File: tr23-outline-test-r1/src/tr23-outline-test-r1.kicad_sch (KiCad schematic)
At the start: 34 parts, among them SW1 REV_TACT, SW10 REV_TACT, SW11 REV_TACT, SW12 REV_TACT, SW13 REV_TACT, SW14 REV_TACT, SW15 REV_TACT, SW16 REV_TACT, SW17 REV_TACT, SW18 REV_TACT, SW19 REV_TACT, SW2 REV_TACT, SW20 REV_TACT, SW21 REV_TACT, SW22 REV_TACT, SW23 REV_TACT, SW24 REV_TACT, SW25 REV_TACT, SW26 REV_TACT, SW27 REV_TACT, SW28 REV_TACT, SW29 REV_TACT, SW3 REV_TACT, SW30 REV_TACT, SW31 REV_TACT, SW32 REV_TACT, SW33 REV_TACT, SW34 REV_TACT, SW4 REV_TACT, SW5 REV_TACT, SW6 REV_TACT, SW7 REV_TACT, SW8 REV_TACT, SW9 REV_TACT

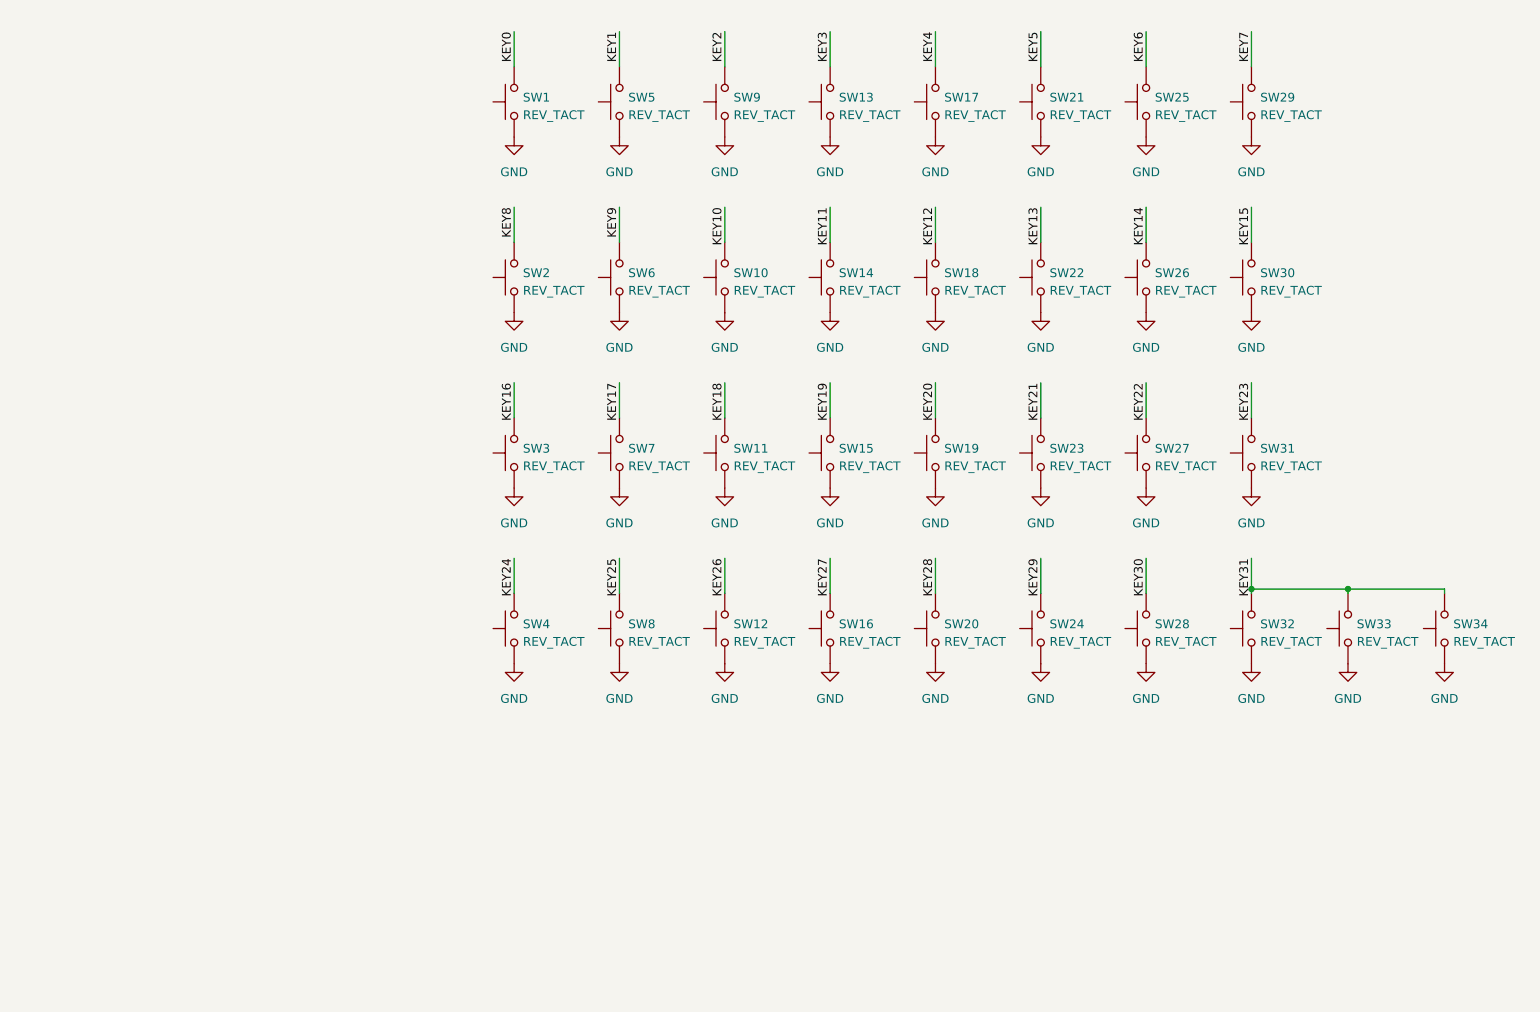
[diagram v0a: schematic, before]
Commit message: Update SVG export
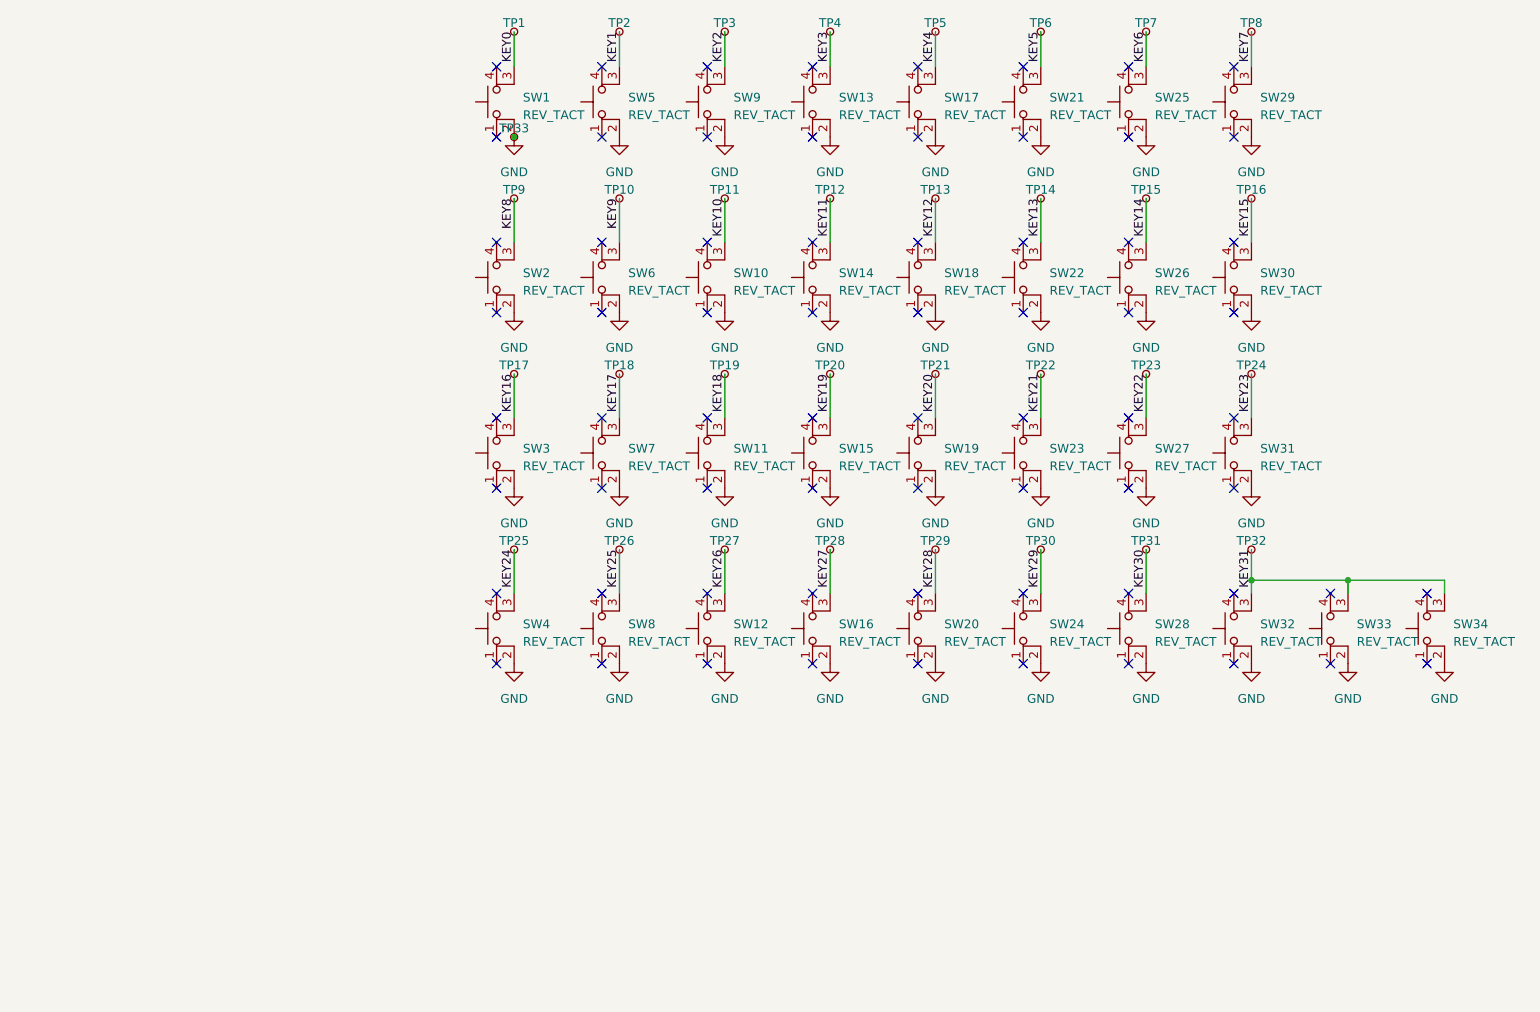
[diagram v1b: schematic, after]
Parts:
- added TP1, TP10, TP11, TP12, TP13, TP14, TP15, TP16, TP17, TP18, TP19, TP2, TP20, TP21, TP22, TP23, TP24, TP25, TP26, TP27, TP28, TP29, TP3, TP30, TP31, TP32, TP33, TP4, TP5, TP6, TP7, TP8, TP9: ~, TestPoint:TestPoint_Pad_D1.5mm, symbol Connector:TestPoint_Small
- SW1, SW10, SW11, SW12, SW13, SW14, SW15, SW16, SW17, SW18, SW19, SW2, SW20, SW21, SW22, SW23, SW24, SW25, SW26, SW27, SW28, SW29, SW3, SW30, SW31, SW32, SW33, SW34, SW4, SW5, SW6, SW7, SW8, SW9: symbol Switch:SW_MEC_5G -> Switch:SW_MEC_5E
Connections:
- net GND: now also TP33.1; no longer SW1.1 (A), SW10.1 (A), SW11.1 (A), SW12.1 (A), SW13.1 (A), SW14.1 (A), SW15.1 (A), SW16.1 (A), SW17.1 (A), SW18.1 (A), SW19.1 (A), SW2.1 (A), SW20.1 (A), SW21.1 (A), SW22.1 (A), SW23.1 (A), SW24.1 (A), SW25.1 (A), SW26.1 (A), SW27.1 (A), SW28.1 (A), SW29.1 (A), SW3.1 (A), SW30.1 (A), SW31.1 (A), SW32.1 (A), SW33.1 (A), SW34.1 (A), SW4.1 (A), SW5.1 (A), SW6.1 (A), SW7.1 (A), SW8.1 (A), SW9.1 (A)
- net KEY0: now also TP1.1; no longer SW1.4 (B)
- net KEY1: now also TP2.1; no longer SW5.4 (B)
- net KEY10: now also TP11.1; no longer SW10.4 (B)
- net KEY11: now also TP12.1; no longer SW14.4 (B)
- net KEY12: now also TP13.1; no longer SW18.4 (B)
- net KEY13: now also TP14.1; no longer SW22.4 (B)
- net KEY14: now also TP15.1; no longer SW26.4 (B)
- net KEY15: now also TP16.1; no longer SW30.4 (B)
- net KEY16: now also TP17.1; no longer SW3.4 (B)
- net KEY17: now also TP18.1; no longer SW7.4 (B)
- net KEY18: now also TP19.1; no longer SW11.4 (B)
- net KEY19: now also TP20.1; no longer SW15.4 (B)
- net KEY2: now also TP3.1; no longer SW9.4 (B)
- net KEY20: now also TP21.1; no longer SW19.4 (B)
- net KEY21: now also TP22.1; no longer SW23.4 (B)
- net KEY22: now also TP23.1; no longer SW27.4 (B)
- net KEY23: now also TP24.1; no longer SW31.4 (B)
- net KEY24: now also TP25.1; no longer SW4.4 (B)
- net KEY25: now also TP26.1; no longer SW8.4 (B)
- net KEY26: now also TP27.1; no longer SW12.4 (B)
- net KEY27: now also TP28.1; no longer SW16.4 (B)
- net KEY28: now also TP29.1; no longer SW20.4 (B)
- net KEY29: now also TP30.1; no longer SW24.4 (B)
- net KEY3: now also TP4.1; no longer SW13.4 (B)
- net KEY30: now also TP31.1; no longer SW28.4 (B)
- net KEY31: now also TP32.1; no longer SW32.4 (B), SW33.4 (B), SW34.4 (B)
- net KEY4: now also TP5.1; no longer SW17.4 (B)
- net KEY5: now also TP6.1; no longer SW21.4 (B)
- net KEY6: now also TP7.1; no longer SW25.4 (B)
- net KEY7: now also TP8.1; no longer SW29.4 (B)
- net KEY8: now also TP9.1; no longer SW2.4 (B)
- net KEY9: now also TP10.1; no longer SW6.4 (B)
- no-connect marks 0 -> 68

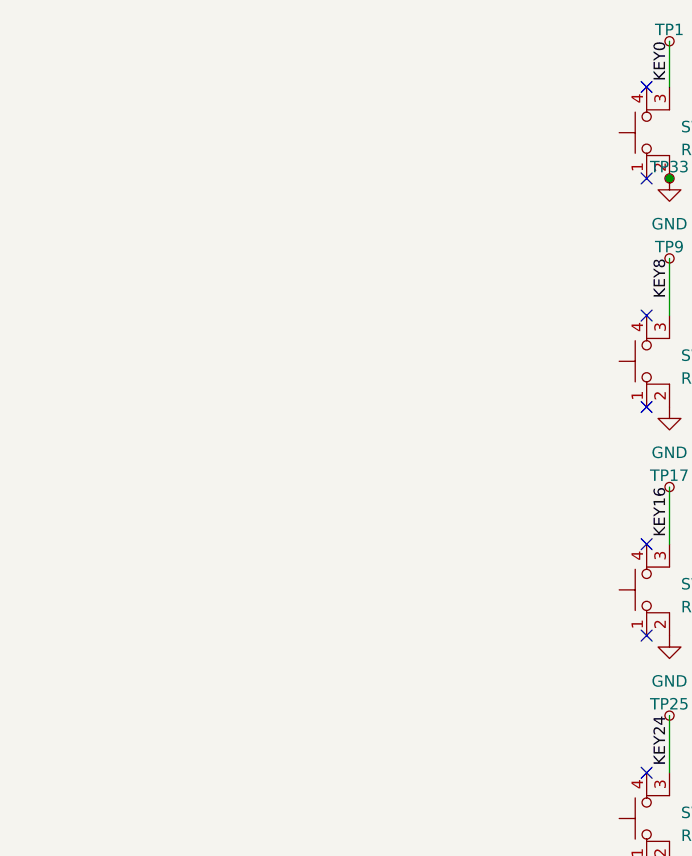
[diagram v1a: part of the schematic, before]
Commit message: Add navigation switches and SAO connector to schematic.
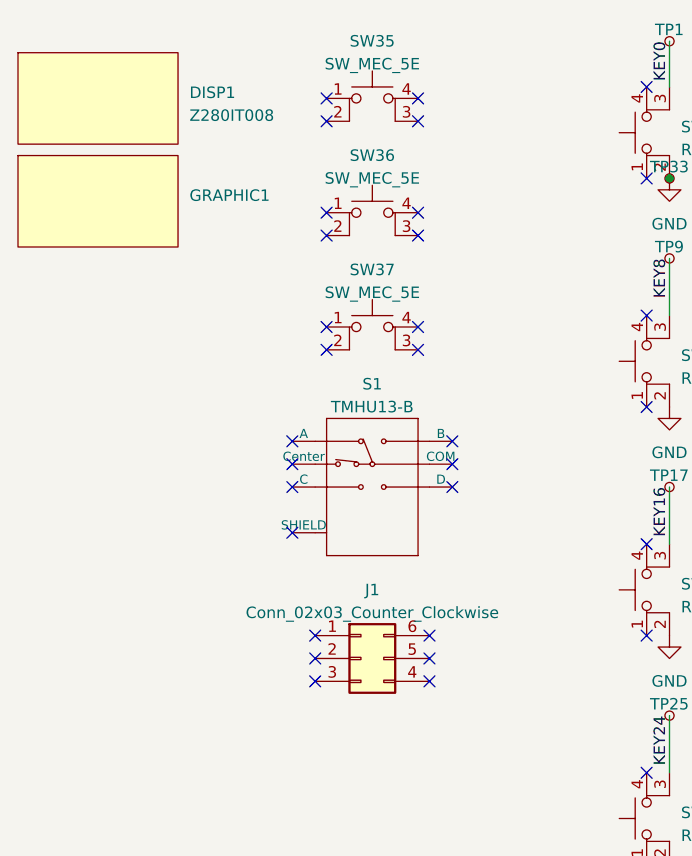
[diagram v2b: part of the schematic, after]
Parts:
- added DISP1: Z280IT008, jeffmakes-kicad-library:Z280IT009, symbol j_Display:Display_dummy
- added GRAPHIC1: (no value), tr23-svg2sz:tr23-r1-svg2sz, symbol j_Display:Display_dummy
- added J1: Conn_02x03_Counter_Clockwise, jeffmakes-kicad-library:PinSocket_2x03_P2.54mm_Through-Board-Mating, symbol Connector_Generic:Conn_02x03_Counter_Clockwise
- added S1: TMHU13-B, jeffmakes-kicad-library:SW_JS1400BFQ, symbol j_Switch:TMHU13-B
- added SW35, SW36, SW37: SW_MEC_5E, jeffmakes-kicad-library:SW_SPST_TACT-6x6-no-silk, symbol Switch:SW_MEC_5E
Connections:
- new net: S1.SH1 (SHIELD), S1.SH2 (SHIELD)
- no-connect marks 68 -> 93

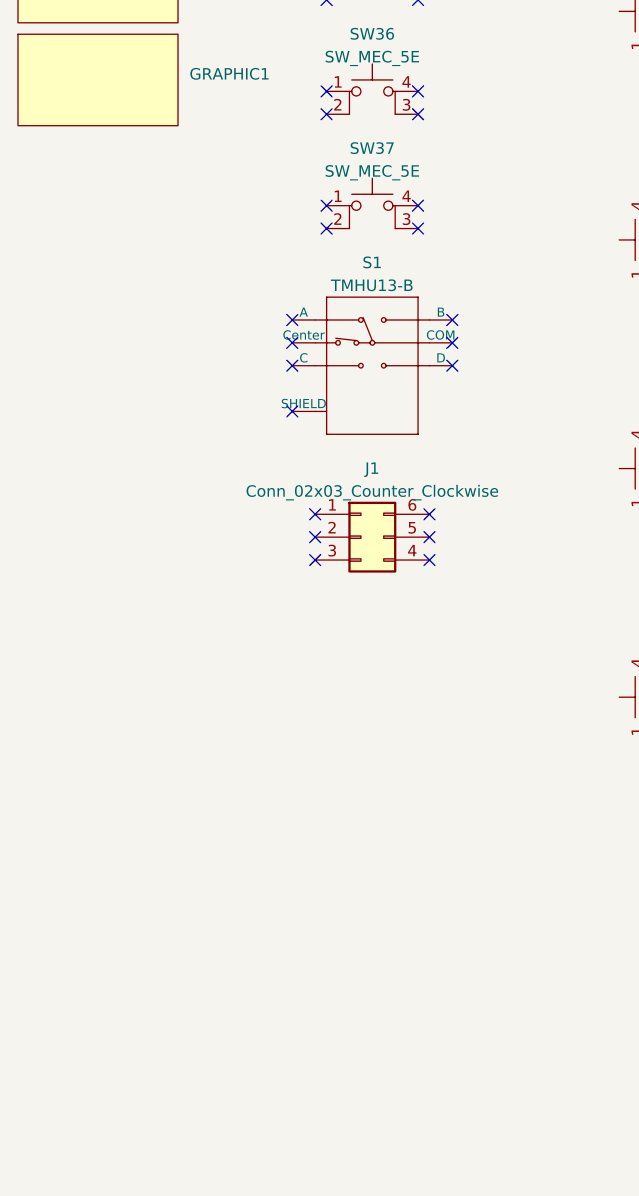
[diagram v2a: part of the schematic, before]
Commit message: Add FFC connector for display.
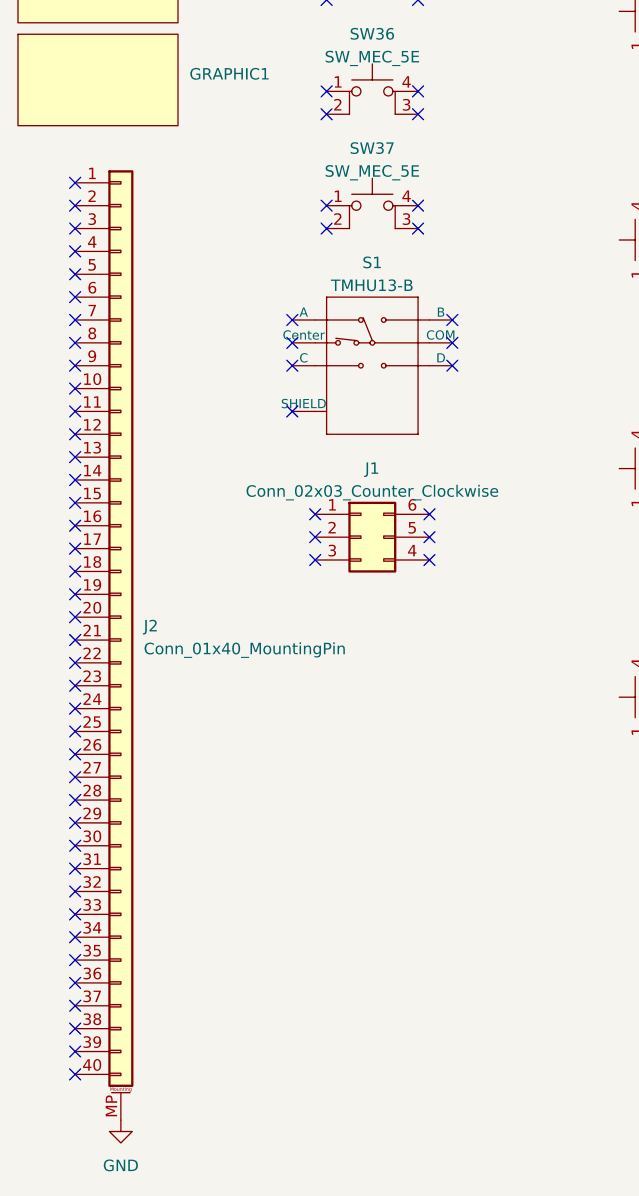
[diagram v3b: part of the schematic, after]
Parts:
- added J2: Conn_01x40_MountingPin, jeffmakes-kicad-library:AFC07x40-1MP_P0.5mm_Horizontal, symbol Connector_Generic_MountingPin:Conn_01x40_MountingPin
- GRAPHIC1: value (none) -> ~
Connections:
- net GND: now also J2.MP (MountPin)
- no-connect marks 93 -> 133
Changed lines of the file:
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@@
   (junction (at 92.71 58.42) (diameter 0) (color 0 0 0 0)
   )
+  (no_connect (at 26.67 82.55))
+  (no_connect (at 26.67 100.33))
   (no_connect (at 210.82 124.46))
   (no_connect (at 53.34 109.22))
@@
   (no_connect (at 196.85 109.22))
   (no_connect (at 50.8 87.63))
+  (no_connect (at 26.67 125.73))
   (no_connect (at 68.58 87.63))
   (no_connect (at 166.37 83.82))
+  (no_connect (at 26.67 77.47))
   (no_connect (at 90.17 58.42))
   (no_connect (at 105.41 109.22))
@@
   (no_connect (at 50.8 90.17))
   (no_connect (at 196.85 99.06))
+  (no_connect (at 26.67 156.21))
   (no_connect (at 105.41 83.82))
   (no_connect (at 66.04 111.76))
+  (no_connect (at 26.67 153.67))
   (no_connect (at 210.82 134.62))
   (no_connect (at 105.41 73.66))
@@
   (no_connect (at 135.89 134.62))
   (no_connect (at 90.17 73.66))
+  (no_connect (at 26.67 102.87))
   (no_connect (at 196.85 48.26))
+  (no_connect (at 26.67 161.29))
   (no_connect (at 54.61 77.47))
   (no_connect (at 151.13 83.82))
+  (no_connect (at 26.67 166.37))
   (no_connect (at 135.89 99.06))
   (no_connect (at 120.65 124.46))
@@
   (no_connect (at 151.13 73.66))
   (no_connect (at 64.77 74.93))
+  (no_connect (at 26.67 90.17))
+  (no_connect (at 26.67 85.09))
+  (no_connect (at 26.67 74.93))
   (no_connect (at 64.77 52.07))
   (no_connect (at 166.37 134.62))
   (no_connect (at 196.85 58.42))
   (no_connect (at 166.37 99.06))
+  (no_connect (at 26.67 92.71))
+  (no_connect (at 26.67 133.35))
   (no_connect (at 53.34 114.3))
+  (no_connect (at 26.67 87.63))
   (no_connect (at 181.61 134.62))
   (no_connect (at 120.65 109.22))
+  (no_connect (at 26.67 123.19))
   (no_connect (at 66.04 109.22))
   (no_connect (at 90.17 83.82))
   (no_connect (at 90.17 134.62))
+  (no_connect (at 26.67 151.13))
   (no_connect (at 181.61 109.22))
+  (no_connect (at 26.67 168.91))
+  (no_connect (at 26.67 113.03))
   (no_connect (at 151.13 124.46))
   (no_connect (at 181.61 99.06))
+  (no_connect (at 26.67 148.59))
   (no_connect (at 64.77 64.77))
   (no_connect (at 135.89 83.82))
@@
   (no_connect (at 105.41 134.62))
   (no_connect (at 54.61 62.23))
+  (no_connect (at 26.67 143.51))
+  (no_connect (at 26.67 128.27))
+  (no_connect (at 26.67 110.49))
   (no_connect (at 166.37 58.42))
+  (no_connect (at 26.67 140.97))
+  (no_connect (at 26.67 80.01))
   (no_connect (at 120.65 134.62))
   (no_connect (at 166.37 124.46))
   (no_connect (at 90.17 48.26))
+  (no_connect (at 26.67 105.41))
   (no_connect (at 105.41 99.06))
   (no_connect (at 135.89 58.42))
@@
   (no_connect (at 135.89 109.22))
   (no_connect (at 64.77 77.47))
+  (no_connect (at 26.67 146.05))
+  (no_connect (at 26.67 130.81))
+  (no_connect (at 26.67 163.83))
   (no_connect (at 68.58 90.17))
+  (no_connect (at 26.67 135.89))
   (no_connect (at 54.61 52.07))
   (no_connect (at 90.17 109.22))
   (no_connect (at 181.61 124.46))
+  (no_connect (at 26.67 118.11))
   (no_connect (at 66.04 114.3))
+  (no_connect (at 26.67 107.95))
   (no_connect (at 151.13 109.22))
   (no_connect (at 135.89 124.46))
+  (no_connect (at 26.67 95.25))
   (no_connect (at 151.13 99.06))
   (no_connect (at 120.65 83.82))
+  (no_connect (at 26.67 171.45))
+  (no_connect (at 26.67 138.43))
   (no_connect (at 135.89 48.26))
   (no_connect (at 224.79 134.62))
@@
   (no_connect (at 54.61 49.53))
   (no_connect (at 64.77 62.23))
+  (no_connect (at 26.67 158.75))
   (no_connect (at 181.61 48.26))
+  (no_connect (at 26.67 115.57))
+  (no_connect (at 26.67 97.79))
   (no_connect (at 120.65 48.26))
   (no_connect (at 151.13 58.42))
   (no_connect (at 166.37 73.66))
+  (no_connect (at 26.67 120.65))
+  (no_connect (at 26.67 72.39))
   (wire (pts (xy 92.71 92.71) (xy 92.71 99.06))
     (stroke (width 0) (type default))
@@
       (effects (font (size 1.27 1.27)) (justify left))
     )
-    (property "Value" "" (at 39.37 62.865 0)
+    (property "Value" "~" (at 39.37 62.865 0)
       (effects (font (size 1.27 1.27)) (justify left))
     )
@@
         )
       )
+    )
+  )
+  (symbol (lib_id "Connector_Generic_MountingPin:Conn_01x40_MountingPin") (at 31.75 120.65 0) (unit 1)
+    (in_bom yes) (on_board yes) (dnp no) (fields_autoplaced)
+    (property "Reference" "J2" (at 34.29 121.6406 0)
+      (effects (font (size 1.27 1.27)) (justify left))
+    )
+    (property "Value" "Conn_01x40_MountingPin" (at 34.29 124.1806 0)
+      (effects (font (size 1.27 1.27)) (justify left))
+    )
+    (property "Footprint" "jeffmakes-kicad-library:AFC07x40-1MP_P0.5mm_Horizontal" (at 31.75 120.65 0)
+      (effects (font (size 1.27 1.27)) hide)
+    )
+    (property "Datasheet" "~" (at 31.75 120.65 0)
+      (effects (font (size 1.27 1.27)) hide)
+    )
+    (pin "1")
+    (pin "10")
+    (pin "11")
+    (pin "12")
+    (pin "13")
+    (pin "14")
+    (pin "15")
+    (pin "16")
+    (pin "17")
+    (pin "18")
+    (pin "19")
+    (pin "2")
+    (pin "20")
+    (pin "21")
+    (pin "22")
+    (pin "23")
+    (pin "24")
+    (pin "25")
+    (pin "26")
+    (pin "27")
+    (pin "28")
+    (pin "29")
+    (pin "3")
+    (pin "30")
+    (pin "31")
+    (pin "32")
+    (pin "33")
+    (pin "34")
+    (pin "35")
+    (pin "36")
+    (pin "37")
+    (pin "38")
+    (pin "39")
+    (pin "4")
+    (pin "40")
+    (pin "5")
+    (pin "6")
+    (pin "7")
+    (pin "8")
+    (pin "9")
+    (pin "MP")
+    (instances
+      (project "tr23-outline-test-r1"
+        (path "/a8e3e111-1bac-465b-987f-3974eb7eae63"
+          (reference "J2") (unit 1)
+        )
+      )
+    )
+  )
+  (symbol (lib_id "power:GND") (at 31.75 176.53 0) (unit 1)
+    (in_bom yes) (on_board yes) (dnp no) (fields_autoplaced)
+    (property "Reference" "#PWR035" (at 31.75 182.88 0)
+      (effects (font (size 1.27 1.27)) hide)
+    )
+    (property "Value" "GND" (at 31.75 181.61 0)
+      (effects (font (size 1.27 1.27)))
+    )
+    (property "Footprint" "" (at 31.75 176.53 0)
+      (effects (font (size 1.27 1.27)) hide)
+    )
+    (property "Datasheet" "" (at 31.75 176.53 0)
+      (effects (font (size 1.27 1.27)) hide)
+    )
+    (pin "1")
+    (instances
+      (project "tr23-outline-test-r1"
+        (path "/a8e3e111-1bac-465b-987f-3974eb7eae63"
+          (reference "#PWR035") (unit 1)
+        )
+      )
+      (project "tr23-badge-r1"
+        (path "/ab725fe7-4504-40ef-b6af-82d065d00fb6/9721eadd-b680-4464-a2f1-ffddf831eebf"
+          (reference "#PWR0103") (unit 1)
+        )
+      )
